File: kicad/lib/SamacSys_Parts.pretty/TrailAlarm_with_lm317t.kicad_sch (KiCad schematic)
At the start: 34 parts

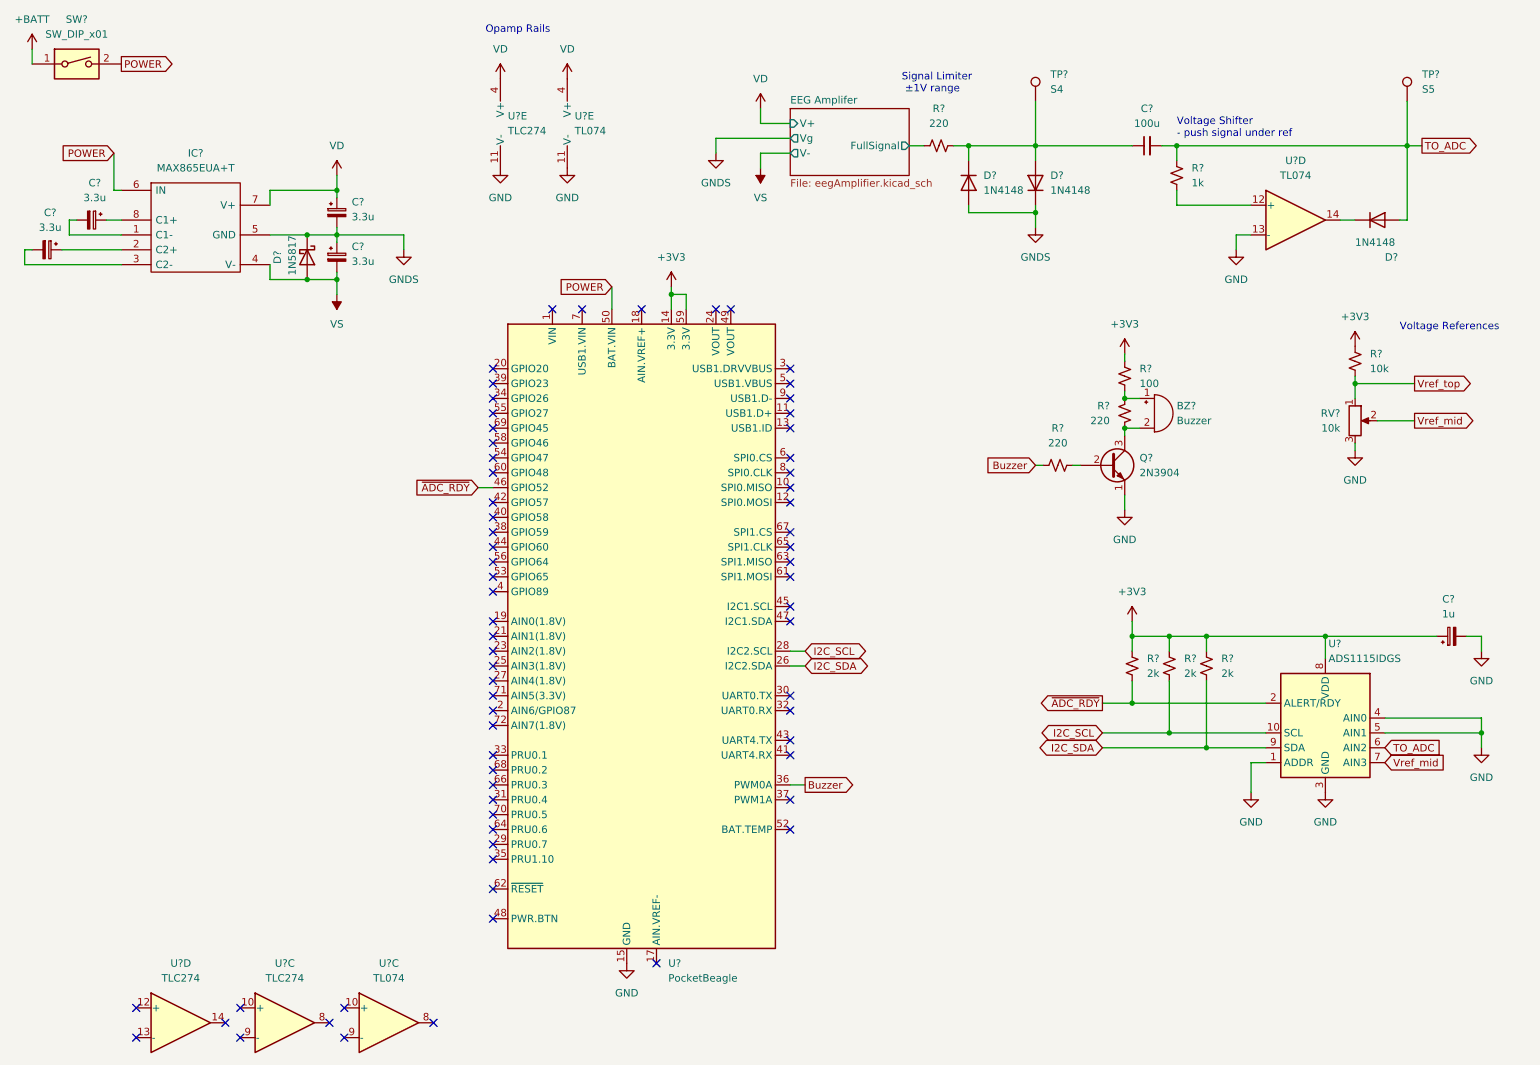
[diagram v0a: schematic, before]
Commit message: Added charge pump to generate rails, switch
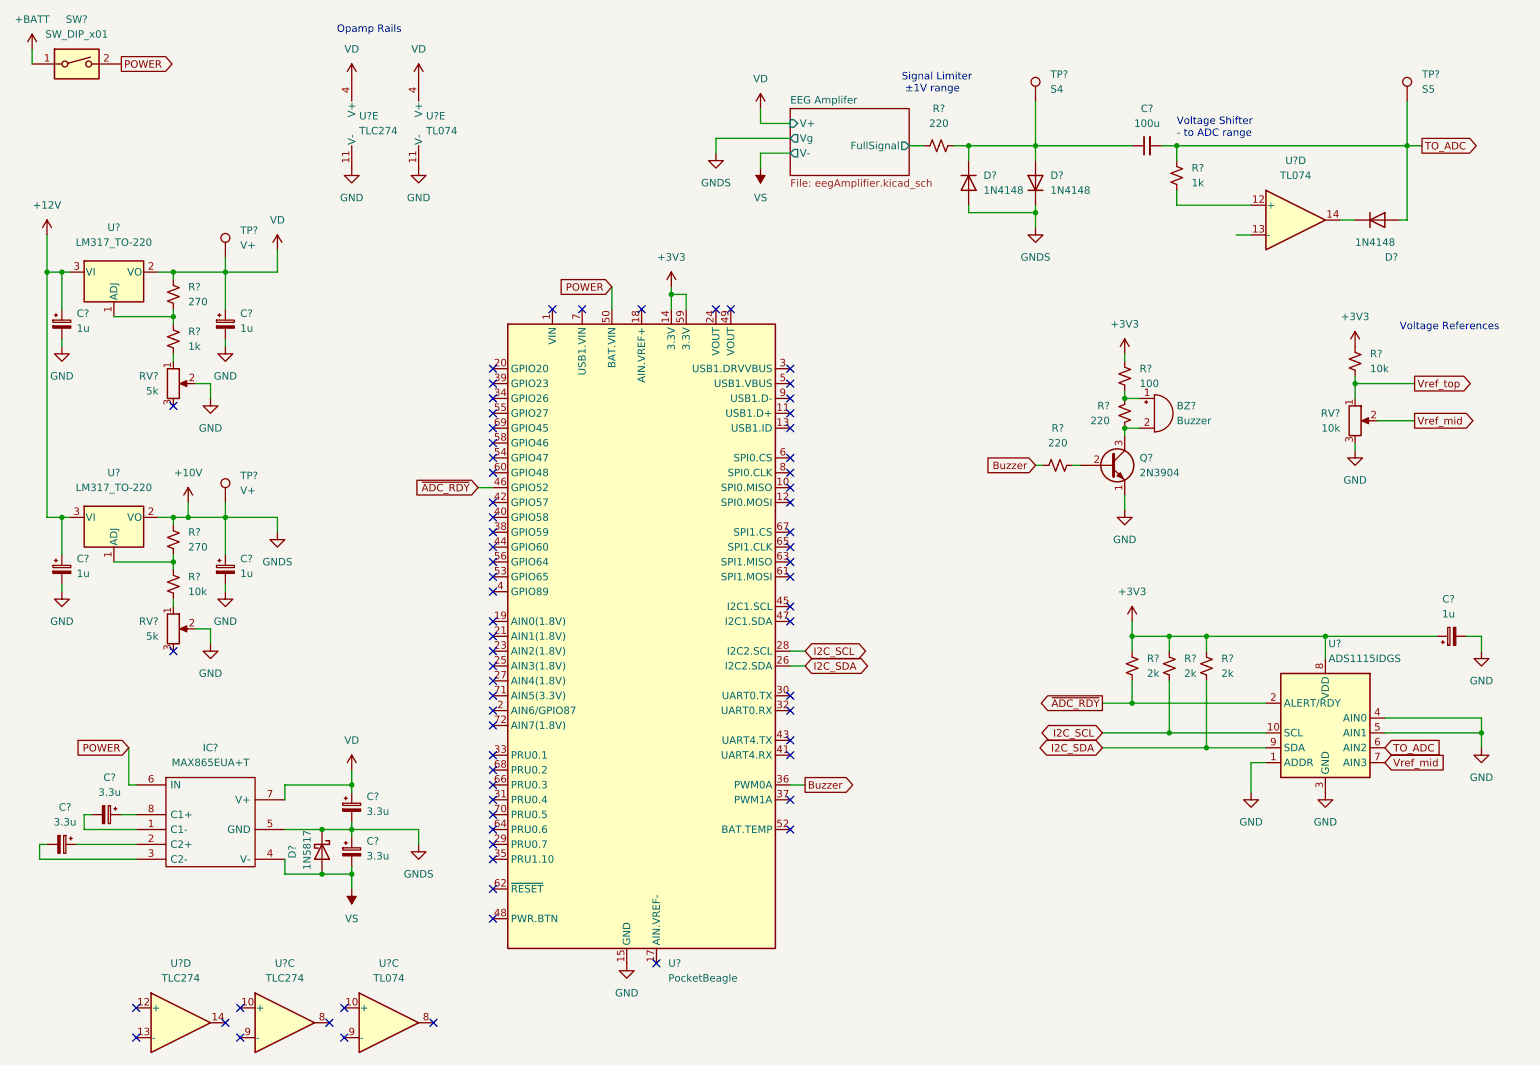
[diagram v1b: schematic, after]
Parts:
- added C? (x4): 1u, symbol Device:C_Polarized_Small
- added R?: 10k, symbol Device:R_Small_US
- added R?: 1k, symbol Device:R_Small_US
- added R? (x2): 270, symbol Device:R_Small_US
- added RV? (x2): 5k, Potentiometer_THT:Potentiometer_Bourns_3266Y_Vertical, symbol Device:R_Potentiometer
- added TP? (x2): V+, symbol Connector:TestPoint
- added U? (x2): LM317_TO-220, Package_TO_SOT_THT:TO-220-3_Vertical, symbol Regulator_Linear:LM317_TO-220
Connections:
- net GND: now also C?.2, C?.2, C?.2, C?.2, RV?.2, RV?.2; no longer U?.13 (-)
- net VD: now also C?.1, R?.1, TP?.1, U?.2 (VO)
- net GNDS renamed +10V
- net +10V: now also C?.1, R?.1, TP?.1, U?.2 (VO)
- new net: R?.1, R?.2, U?.1 (ADJ) (x2)
- new net: R?.2, RV?.1 (x2)
- new net +12V: C?.1, C?.1, U?.3 (VI), U?.3 (VI)
- no-connect marks 69 -> 71
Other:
- note added: "Voltage Shifter - to ADC range"
- note removed: "Voltage Shifter - push signal under ref"
- moved on the sheet: C?, D?, IC?, U?E
